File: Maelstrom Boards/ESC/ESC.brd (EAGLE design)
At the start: 101.6 x 101.6 mm, 27 parts

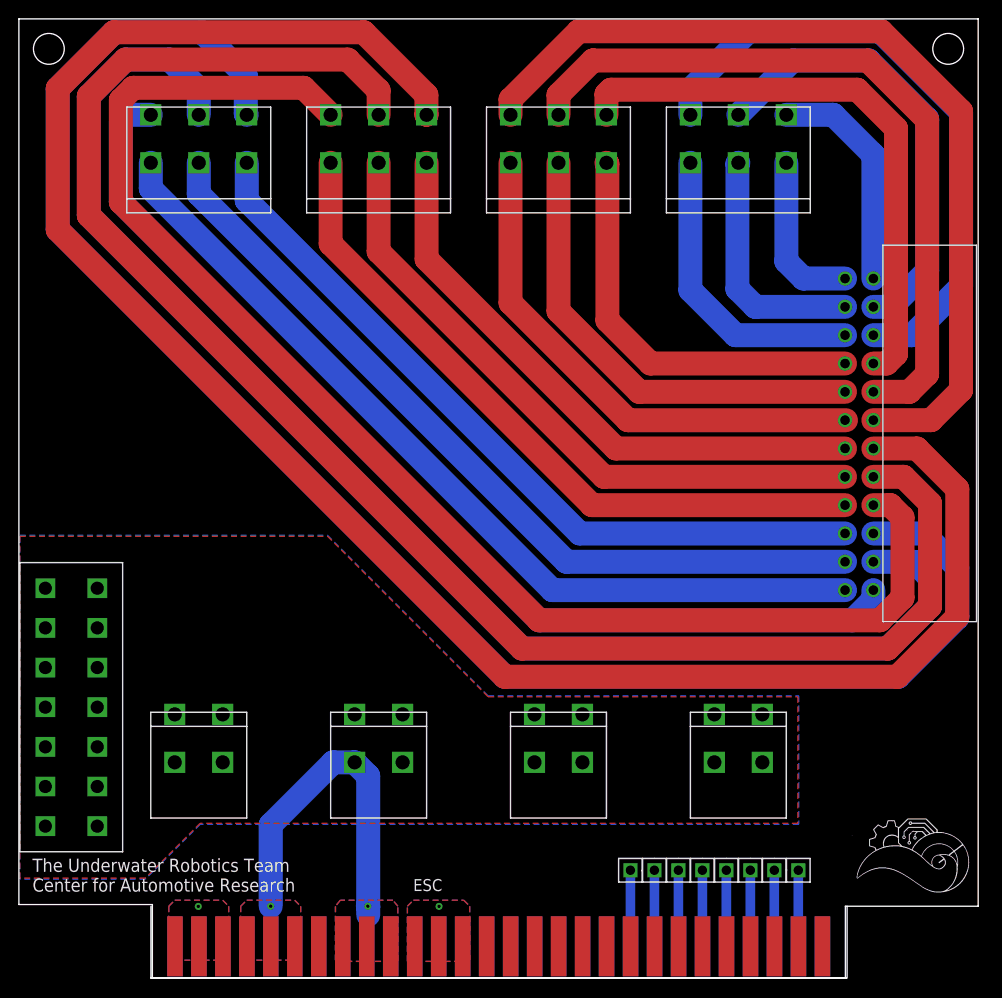
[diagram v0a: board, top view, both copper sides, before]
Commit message: Added LEDs onto ESC board
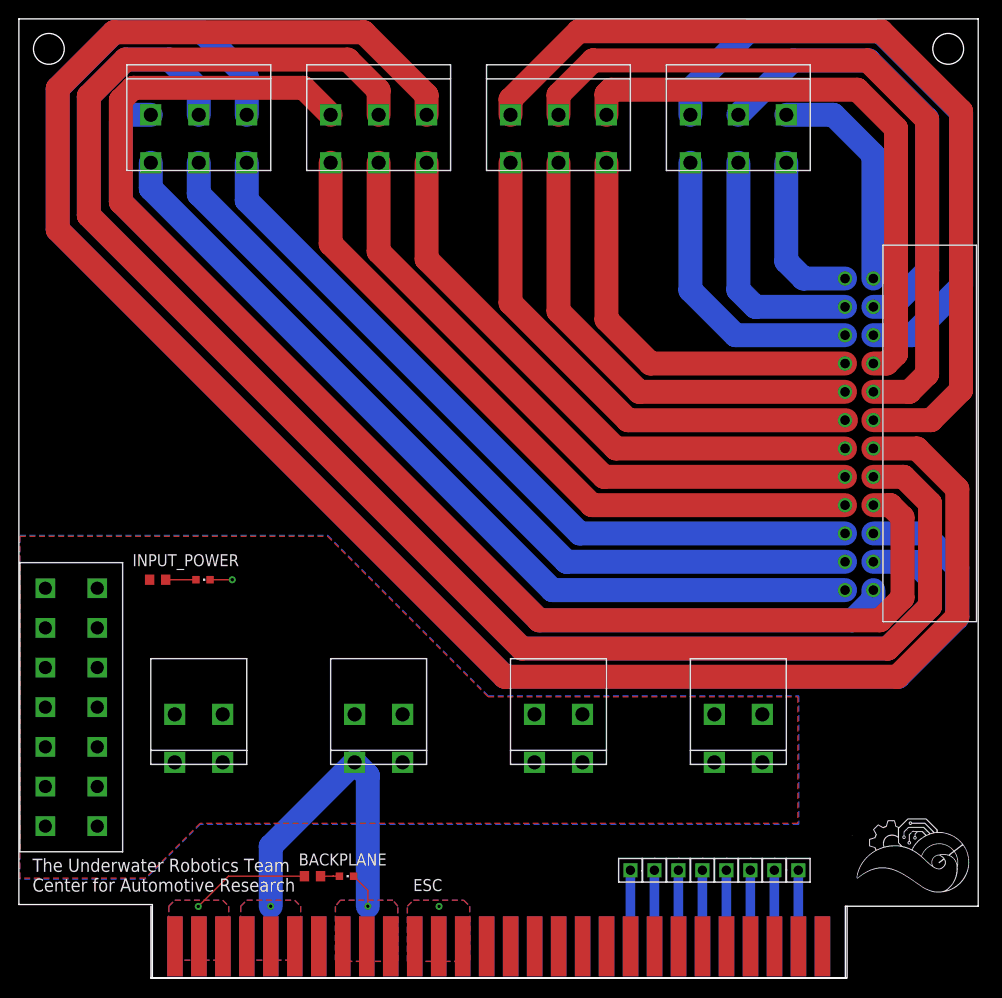
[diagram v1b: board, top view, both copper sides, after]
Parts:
- added BACKPLANE, INPUT_POWER: (no value), led:CHIPLED_0603
- added R1, R2: (no value), resistor:R0603
- flipped 1 to the bottom, turned to 180 degrees
- flipped 2 to the top, turned to 180 degrees
- flipped 3 to the bottom, turned to 180 degrees
- flipped 4 to the top, turned to 180 degrees
- flipped 5 to the bottom, turned to 180 degrees
- flipped 6 to the top, turned to 180 degrees
- flipped 7 to the bottom, turned to 180 degrees
- flipped 8 to the top, turned to 180 degrees
- flipped U$2 to the bottom, turned to 180 degrees
- flipped U$3 to the bottom, turned to 180 degrees
- flipped U$4 to the top, turned to 180 degrees
- flipped U$5 to the top, turned to 180 degrees
- flipped U$6 to the top, turned to 180 degrees
- flipped U$7 to the top, turned to 180 degrees
- flipped U$8 to the bottom, turned to 180 degrees
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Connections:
- new net N$25: INPUT_POWER.A, R1.2
- new net N$26: BACKPLANE.A, R2.2
- net +3V3: now also R2.1
- net BALANCED+: now also R1.1
- net GND: now also BACKPLANE.C, INPUT_POWER.C
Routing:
- net +3V3: track 0.00 -> 12.6 mm
- net GND: track 37.1 -> 41.8 mm, vias 2 -> 3
- net N$25: track 0.00 -> 3.20 mm
- net N$26: track 0.00 -> 2.00 mm

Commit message: Moved LED to not interfere with ESC placement, added labels to bNames and tNames for the PWM signals and for each ESC, and parts moved so plastic does not overlap with a pad.
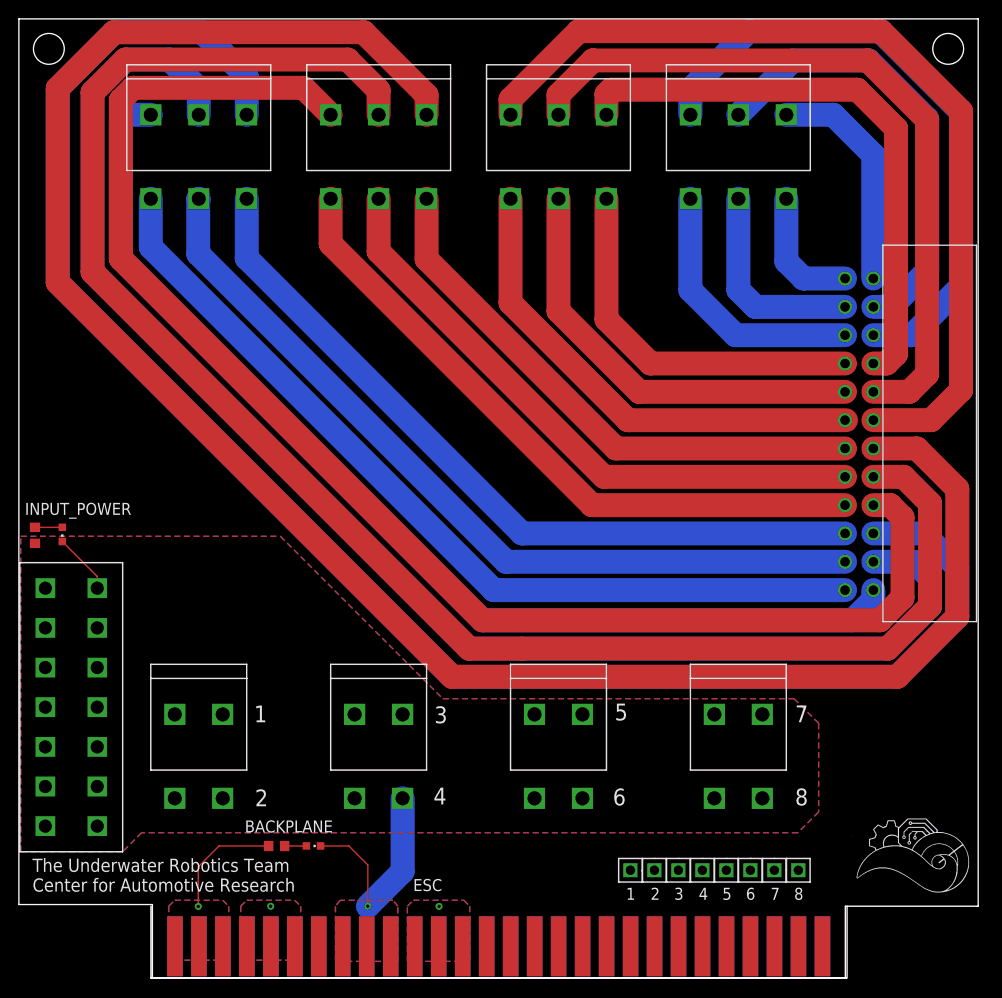
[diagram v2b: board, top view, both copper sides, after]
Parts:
- moved INPUT_POWER 15.7 mm to (4.60, 47.0), turned to 180 degrees
- moved R1 13.8 mm to (1.70, 46.9), turned to 90 degrees
- moved R2 4.97 mm to (27.3, 14.0)
- moved BACKPLANE 4.74 mm to (31.2, 14.0)
- moved 1 3.81 mm to (76.2, 82.5)
- moved 3 3.81 mm to (57.1, 82.5)
- moved 5 3.81 mm to (38.1, 82.5)
- moved 7 3.81 mm to (19.1, 82.5)
- moved U$2 3.81 mm to (76.2, 19.1), turned to 0 degrees
- moved U$3 3.81 mm to (38.1, 19.1), turned to 0 degrees
- moved U$8 3.81 mm to (19.1, 19.1), turned to 0 degrees
- moved U$9 3.81 mm to (57.1, 19.1), turned to 0 degrees
- turned U$4 to 0 degrees
- turned U$5 to 0 degrees
- turned U$6 to 0 degrees
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- renumbered U$24 to P5, U$25 to P6, U$26 to P7, U$27 to P8
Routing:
- net GND: track 41.8 -> 29.6 mm, vias 3 -> 2
- net PWM_5: track 8.09 -> 0.00 mm
- net PWM_6: track 8.07 -> 0.00 mm
- net PWM_4: track 8.07 -> 0.00 mm
- net PWM_8: track 8.11 -> 0.05 mm
- net PWM_3: track 8.11 -> 0.07 mm
- net PWM_2: track 8.17 -> 0.13 mm
- net PWM_1: track 9.06 -> 1.02 mm
- net PWM_7: track 8.07 -> 0.04 mm
- net N$9: track 55.5 -> 51.7 mm
- net N$8: track 49.6 -> 45.8 mm
- net N$7: track 43.8 -> 40.0 mm
- net N$3: track 31.8 -> 28.0 mm
- net N$2: track 25.5 -> 21.7 mm
- net N$15: track 74.5 -> 70.7 mm
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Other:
- board text added: "1"
- board text added: "2"
- board text added: "3"
- board text added: "4"
- board text added: "5"
- board text added: "6"
- board text added: "7"
- board text added: "8"

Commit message: Finished ESC board, need to go back for minor changes.
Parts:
- removed U$2, U$3, U$4, U$5, U$6, U$7, U$8, U$9: 1711725, Screw_Terminals:1711725
- added 1C, 2C, 3C, 4C, 5C, 6C, 7C, 8C: ACS722, ACS722:SOIC-8
- added 1CONNECT, 2CONNECT, 3CONNECT, 4CONNECT, 5CONNECT, 7CONNECT, 8CONNECT, CONNECT: 1711725, Screw_Terminals:1711725
- added C1, C2, C3, C4, C5, C6, C7, C8, C9: (no value), rcl:C0603
- added R3, R4, R5, R6: (no value), resistor:R0603
- added U$24: ADC128D818, ADC128D818:TSSOP-16
- moved 1 57.8 mm to (19.1, 91.4), flipped to the top, turned to 0 degrees
- moved 2 57.8 mm to (19.1, 82.5), flipped to the bottom, turned to 0 degrees
- moved 7 57.8 mm to (76.2, 91.4), flipped to the top, turned to 0 degrees
- moved 8 57.8 mm to (76.2, 82.5), flipped to the bottom, turned to 0 degrees
- moved 3 21.0 mm to (38.1, 91.4), flipped to the top, turned to 0 degrees
- moved 4 21.0 mm to (38.1, 82.5), flipped to the bottom, turned to 0 degrees
- moved 5 21.0 mm to (57.1, 91.4), flipped to the top, turned to 0 degrees
- moved 6 21.0 mm to (57.1, 82.5), flipped to the bottom, turned to 0 degrees
- moved BACKPLANE 10.5 mm to (21.4, 10.3)
- moved R2 10.2 mm to (17.8, 10.3)
- moved P5 1.78 mm to (74.9, 9.65)
- moved P6 1.78 mm to (77.5, 9.65)
- moved P7 1.78 mm to (80.0, 9.65)
- moved P8 1.78 mm to (82.5, 9.65)
- moved U$20 1.78 mm to (64.8, 9.65)
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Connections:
- new net 0ADC: 1C.VIOUT, U$24.IN0
- new net 1ADC: 2C.VIOUT, U$24.IN1
- new net 2ADC: 3C.VIOUT, U$24.IN2
- new net 3ADC: 4C.VIOUT, U$24.IN3
- new net 4ADC: 5C.VIOUT, U$24.IN4
- new net 5ADC: 6C.VIOUT, U$24.IN5
- new net 6ADC: 7C.VIOUT, U$24.IN6
- new net 7ADC: 8C.VIOUT, U$24.IN7
- new net N$30: 1C.IP-1, 1C.IP-2, 1CONNECT.RED
- new net N$32: 2C.IP+1, 2C.IP+2, 2CONNECT.BLACK
- new net N$33: 3C.IP-1, 3C.IP-2, 3CONNECT.RED
- new net N$34: 5C.IP-1, 5C.IP-2, 5CONNECT.RED
- new net N$35: 4C.IP+1, 4C.IP+2, 4CONNECT.BLACK
- new net N$36: 6C.IP+1, 6C.IP+2, CONNECT.BLACK
- new net N$37: 7C.IP-1, 7C.IP-2, 7CONNECT.RED
- new net N$38: 8C.IP+1, 8C.IP+2, 8CONNECT.BLACK
- new net N$44: R3.2, R4.1, U$24.A0
- new net N$46: R5.1, R6.2, U$24.A1
- new net SCL: U$1.31, U$24.SCL
- new net SDA: U$1.32, U$24.SDA
- net +3V3: now also 1C.VCC, 2C.VCC, 3C.VCC, 4C.VCC, 5C.VCC, 6C.VCC, 7C.VCC, 8C.VCC, C1.2, C2.2, C3.2, C4.2, C5.2, C6.2, C7.2, C8.2, C9.1, R3.1, R6.1, U$24.V+, U$24.VREF
- net BALANCED+: now also 1C.IP+1, 1C.IP+2, 2CONNECT.RED, 3C.IP+1, 3C.IP+2, 4CONNECT.RED, 5C.IP+1, 5C.IP+2, 7C.IP+1, 7C.IP+2, 8CONNECT.RED, CONNECT.RED; no longer U$2.RED, U$3.RED, U$4.RED, U$5.RED, U$6.RED, U$7.RED, U$8.RED, U$9.RED
- net GND: now also 1C.BW_SEL, 1C.GND, 1CONNECT.BLACK, 2C.BW_SEL, 2C.GND, 2C.IP-1, 2C.IP-2, 3C.BW_SEL, 3C.GND, 3CONNECT.BLACK, 4C.BW_SEL, 4C.GND, 4C.IP-1, 4C.IP-2, 5C.BW_SEL, 5C.GND, 5CONNECT.BLACK, 6C.BW_SEL, 6C.GND, 6C.IP-1, 6C.IP-2, 7C.BW_SEL, 7C.GND, 7CONNECT.BLACK, 8C.BW_SEL, 8C.GND, 8C.IP-1, 8C.IP-2, C1.1, C2.1, C3.1, C4.1, C5.1, C6.1, C7.1, C8.1, C9.2, R4.2, R5.2, U$24.GND; no longer U$2.BLACK, U$3.BLACK, U$4.BLACK, U$5.BLACK, U$6.BLACK, U$7.BLACK, U$8.BLACK, U$9.BLACK
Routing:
- net +3V3: track 12.6 -> 182.9 mm, vias 1 -> 7
- net N$4: track 179.8 -> 13.7 mm
- net N$9: track 206.3 -> 40.4 mm
- net N$17: track 40.0 -> 204.3 mm
- net N$22: track 13.6 -> 170.5 mm
- net N$8: track 179.8 -> 46.1 mm
- net N$18: track 45.8 -> 177.9 mm
- net N$3: track 152.5 -> 21.9 mm
- net N$1: track 21.7 -> 145.2 mm
- net GND: track 29.6 -> 149.1 mm, vias 2 -> 13
- net N$7: track 152.5 -> 52.2 mm
- net N$16: track 51.7 -> 151.0 mm
- net N$24: track 28.0 -> 114.7 mm
- net N$2: track 115.5 -> 29.1 mm
- net 0ADC: track 0.00 -> 75.0 mm
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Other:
- board text added: "THRUSTER OUTPUT"

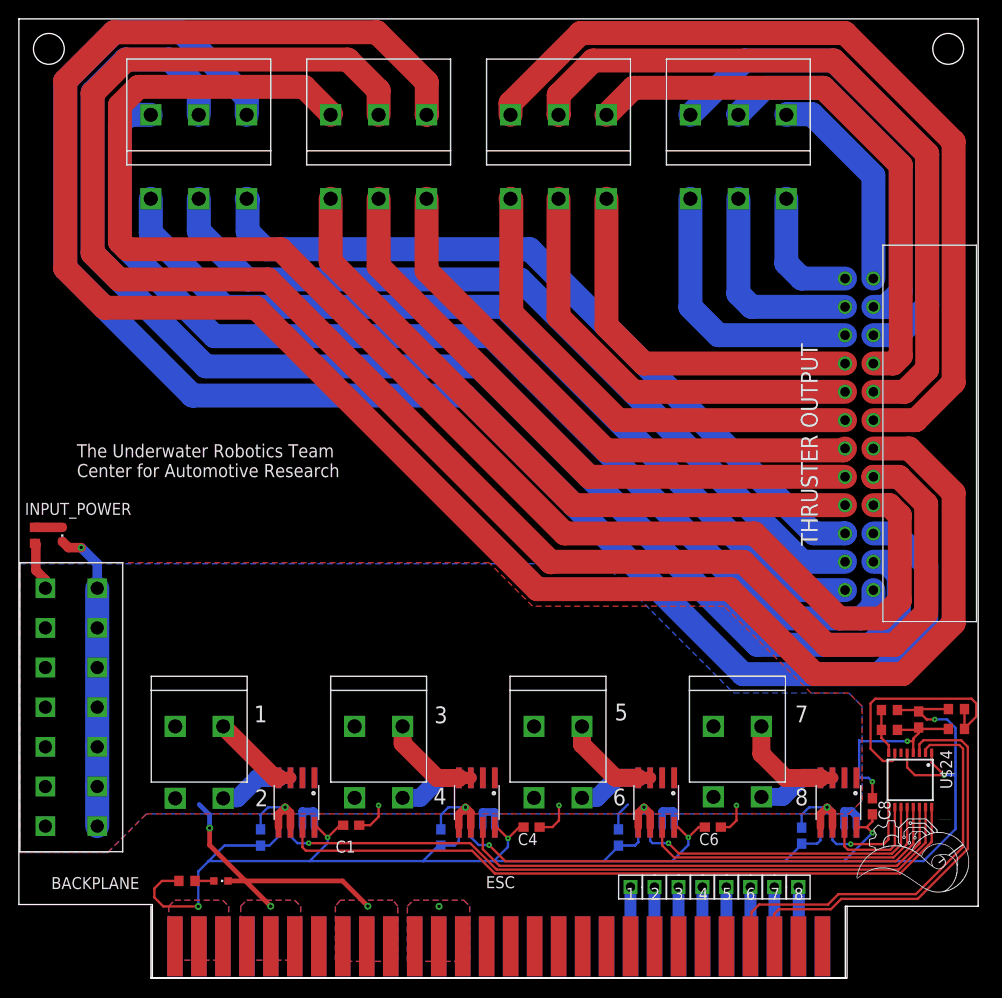
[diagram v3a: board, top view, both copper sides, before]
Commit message: Rerouted current sensors and added bypass capacitors to ADC
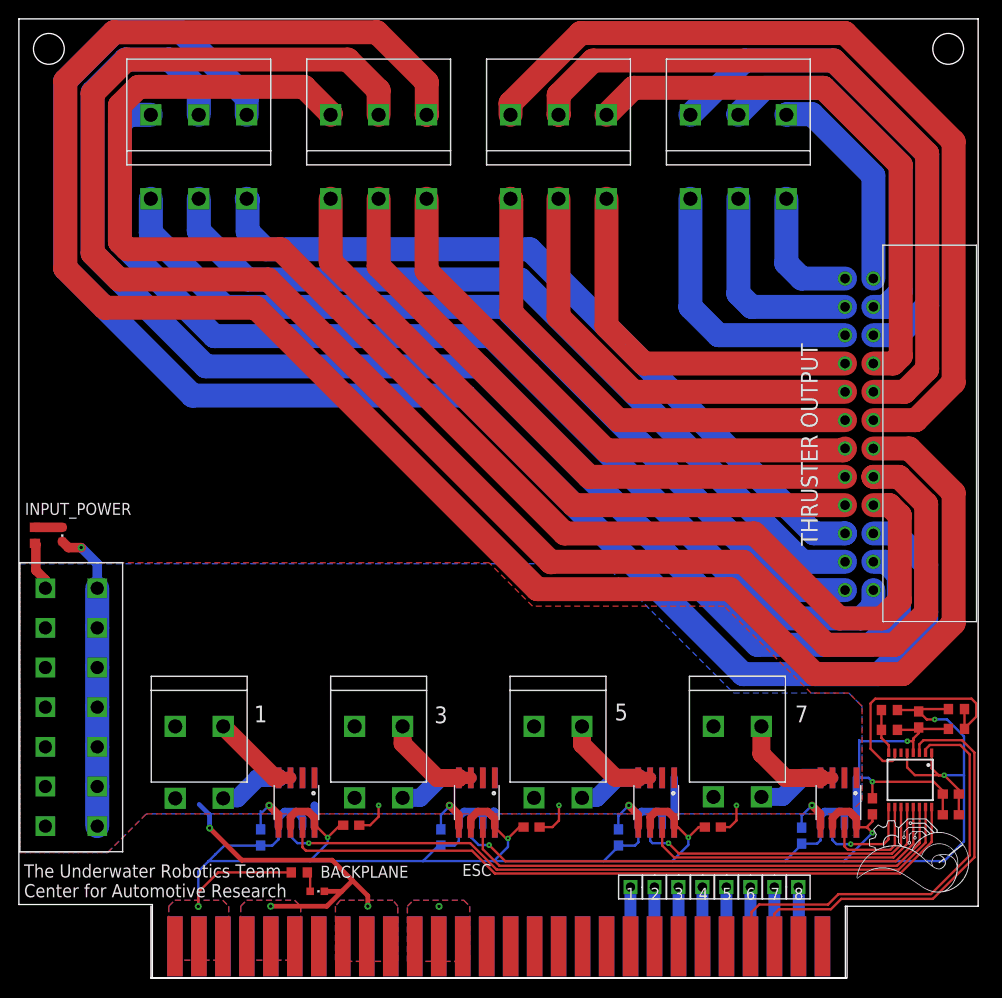
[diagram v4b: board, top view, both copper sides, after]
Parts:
- added C10, C11: (no value), rcl:C0603
- moved R2 11.9 mm to (29.7, 11.2)
- moved BACKPLANE 10.3 mm to (31.6, 9.20)
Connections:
- net +3V3: now also 1C.BW_SEL, 2C.BW_SEL, 3C.BW_SEL, 4C.BW_SEL, 5C.BW_SEL, 6C.BW_SEL, 7C.BW_SEL, 8C.BW_SEL, C10.2, C11.2
- net GND: now also C10.1, C11.1; no longer 1C.BW_SEL, 2C.BW_SEL, 3C.BW_SEL, 4C.BW_SEL, 5C.BW_SEL, 6C.BW_SEL, 7C.BW_SEL, 8C.BW_SEL
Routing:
- net +3V3: track 182.9 -> 236.0 mm
- net SDA: track 44.0 -> 45.6 mm
- net SCL: track 44.1 -> 45.7 mm

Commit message: Updated schematic/board with labels and added capacitor values.
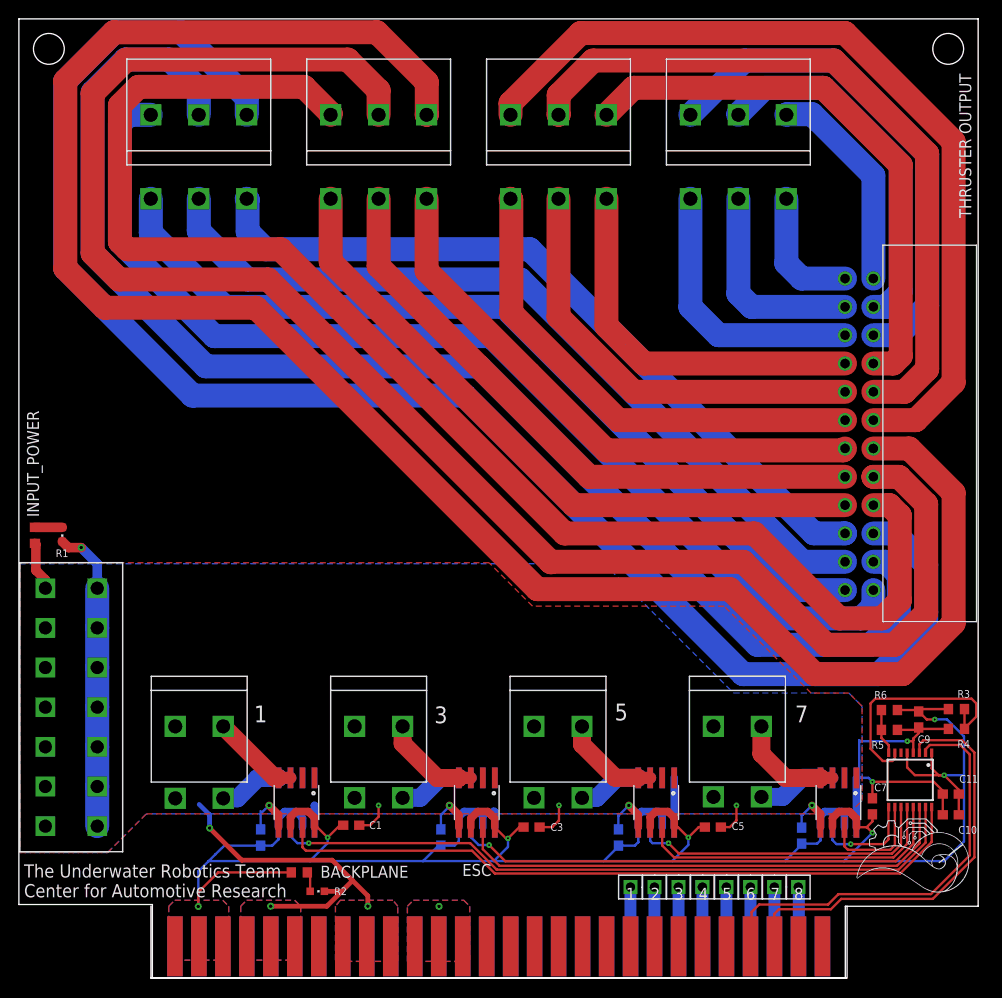
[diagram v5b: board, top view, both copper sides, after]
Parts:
- C1, C10, C2, C3, C4, C5, C6, C7, C8: value (none) -> 0.1uF
- C11: value (none) -> 1uF
- moved C7 27.1 mm to (90.4, 18.2), flipped to the top
- moved C6 10.1 mm to (63.5, 14.9), flipped to the bottom, turned to 270 degrees
- moved C3 9.66 mm to (54.3, 16.0), flipped to the top, turned to 180 degrees
- moved C4 9.66 mm to (44.7, 14.9), flipped to the bottom, turned to 270 degrees
- moved C5 9.44 mm to (73.5, 16.0), flipped to the top, turned to 180 degrees
- moved C8 8.12 mm to (82.9, 15.1), flipped to the bottom
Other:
- board text added: "C1"
- board text added: "C10"
- board text added: "C11"
- board text added: "C2"
- board text added: "C3"
- board text added: "C4"
- board text added: "C5"
- board text added: "C6"
- board text added: "C7"
- board text added: "C8"
- board text added: "C9"
- board text added: "R1"
- board text added: "R2"
- board text added: "R3"
- board text added: "R4"
- board text added: "R5"
- board text added: "R6"
